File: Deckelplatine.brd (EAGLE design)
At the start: 110 x 75 mm, 61 parts, among them IC1 MAX1487EESA+, IC2 74HCT595D, IC3 74HCT595D, IC4 74HCT595D, IC5 74HCT595D, IC6 74HCT595D, J1 52808-2570, Q1 BC846BSMD, Q2 BC846BSMD, U1 LM2676S, X1 236-404, X2 233-502

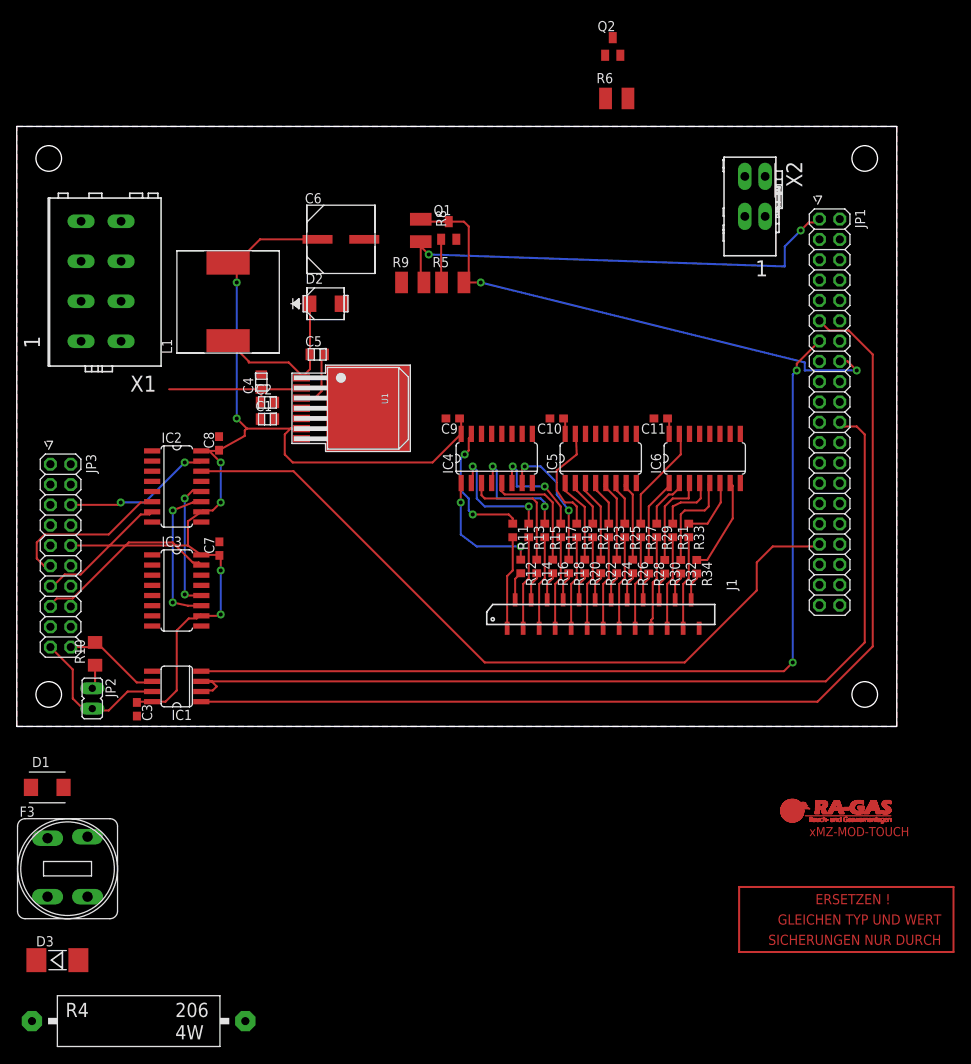
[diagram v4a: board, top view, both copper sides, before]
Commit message: Schema, Board Layout und Routing komplett
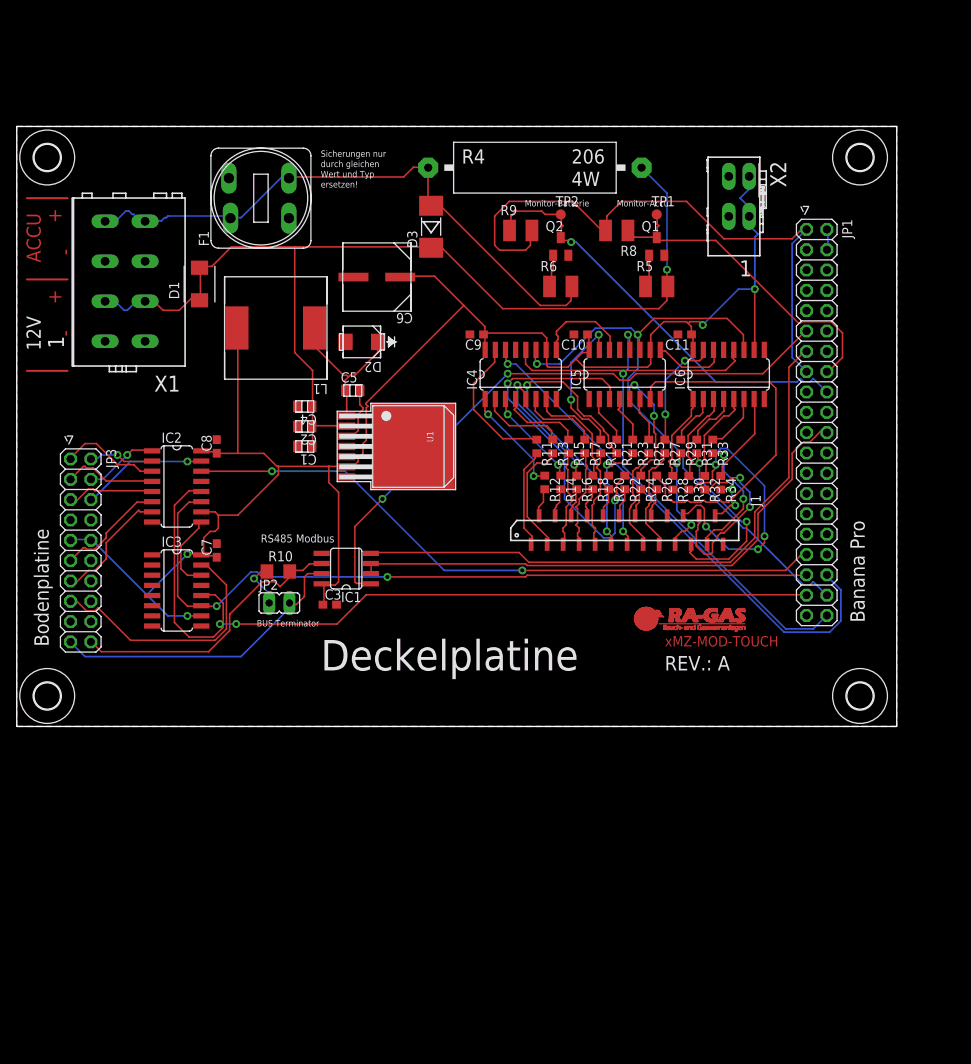
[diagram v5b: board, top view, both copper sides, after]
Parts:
- removed F3: 0.63AT, fuse-schurter:3101.0040
- added F1: FPG4-3101.0040, fuse-schurter:3101.0040
- added H1, H2, H3, H4: MOUNT-HOLE3.3, holes:3,3
- added TP1, TP2: TPSB1,27, testpad:B1,27
- moved R4 117.6 mm to (64.8, 69.8)
- moved D3 102.9 mm to (51.8, 62.5), turned to 90 degrees
- moved D1 65.7 mm to (22.9, 55.3), turned to 90 degrees
- moved C3 27.4 mm to (39.1, 15.2), turned to 0 degrees
- moved JP2 26.3 mm to (32.8, 15.4), turned to 270 degrees
- moved Q1 26.1 mm to (80.0, 60.0)
- moved Q2 25.8 mm to (68.0, 60.0)
- moved IC1 25.8 mm to (41.2, 19.7)
- moved R5 25.5 mm to (80.0, 55.0)
- moved R10 25.1 mm to (32.7, 19.4), turned to 0 degrees
- moved R6 24.5 mm to (68.0, 55.0)
- moved R8 24.5 mm to (75.0, 62.0), turned to 180 degrees
- moved R9 15.0 mm to (63.0, 62.0)
- moved C10 10.9 mm to (70.5, 49.0)
- moved C11 10.9 mm to (83.5, 49.0)
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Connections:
- removed net ACCU-: X1.L4.1, X1.L4.2
- removed net N$38: D3.A, F3.4, R4.1
- removed net N$39: F3.1
- removed net V+: D3.C, R4.2
- net !MON_BAT: now also TP2.TP; no longer R6.2
- net !MON_MAINS: now also TP1.TP; no longer R5.2
- net 12V_VIN: now also D3.C, R4.2, R5.2, X1.L2.1, X1.L2.2; no longer X1.L1.1, X1.L1.2
- net ACCU+: now also D3.A, F1.1, F1.4, R4.1, R6.2, X1.L4.1, X1.L4.2; no longer X1.L3.1, X1.L3.2
- net GND: now also X1.L1.1, X1.L1.2, X1.L3.1, X1.L3.2; no longer X1.L2.1, X1.L2.2
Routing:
- net 12V_VIN: track 18.1 -> 129.6 mm, vias 0 -> 1
- net REL_RCK: track 16.7 -> 107.6 mm
- net LED_RCK: track 0.00 -> 84.1 mm, vias 0 -> 2
- net VCC: track 144.8 -> 226.0 mm, vias 6 -> 4
- net LED_SCK: track 0.00 -> 80.4 mm, vias 0 -> 2
- net REL_SCK: track 18.9 -> 95.2 mm
- net ACCU+: track 0.00 -> 74.3 mm
- net N$1413: track 69.8 -> 0.00 mm
- net LED_SER: track 0.00 -> 64.5 mm, vias 0 -> 1
- net RXD: track 131.7 -> 76.2 mm, vias 0 -> 2
- net !MON_BAT: track 0.00 -> 53.6 mm, vias 0 -> 1
- net RTS: track 118.9 -> 69.1 mm
- net TXD: track 115.9 -> 76.0 mm, vias 2 -> 0
- net N$17: track 10.4 -> 48.8 mm, vias 0 -> 2
- net N$22: track 10.1 -> 46.2 mm
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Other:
- board text added: "+"
- board text added: "-"
- board text added: "12V"
- board text added: "ACCU"
- board text added: "BUS Terminator"
- board text added: "Banana Pro"
- board text added: "Bodenplatine"
- board text added: "Deckelplatine"
- board text added: "Monitor-Accu"
- board text added: "Monitor-Batterie"
- board text added: "REV.: A"
- board text added: "RS485 Modbus"
- board text added: "Sicherungen nur durch gleichen Wert und Typ ersetzen!"
- board text removed: "ERSETZEN !"
- board text removed: "GLEICHEN TYP UND WERT"
- board text removed: "SICHERUNGEN NUR DURCH"

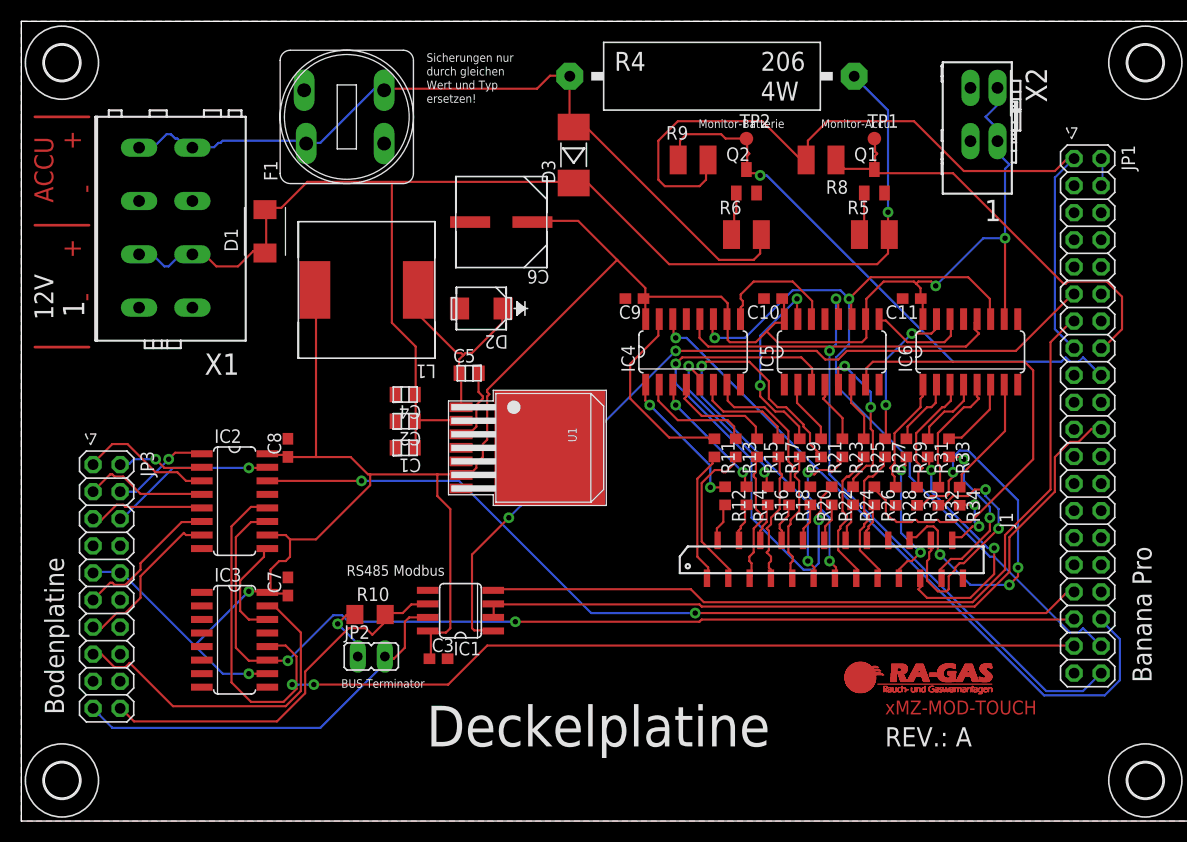
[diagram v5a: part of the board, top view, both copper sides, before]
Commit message: Autorouter mit 7 Airwire left
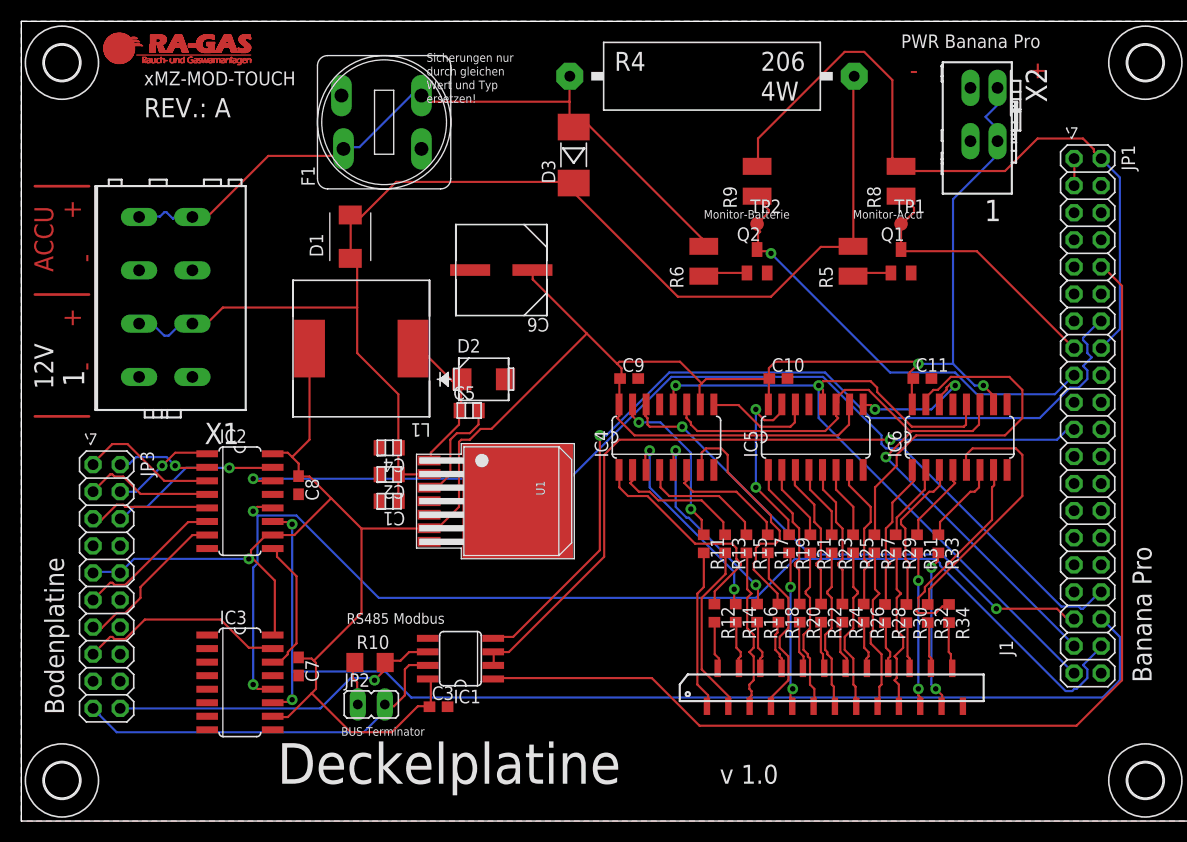
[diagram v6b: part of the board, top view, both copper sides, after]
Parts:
- moved J1 12.0 mm to (76.0, 12.5)
- moved R12 11.0 mm to (65.0, 19.5)
- moved R14 11.0 mm to (67.0, 19.5)
- moved R16 11.0 mm to (69.0, 19.5)
- moved R18 11.0 mm to (71.0, 19.5)
- moved R20 11.0 mm to (73.0, 19.5)
- moved R22 11.0 mm to (75.0, 19.5)
- moved R24 11.0 mm to (77.0, 19.5)
- moved R26 11.0 mm to (79.0, 19.5)
- moved R28 11.0 mm to (81.0, 19.5)
- moved R30 11.0 mm to (83.0, 19.5)
- moved R32 11.0 mm to (85.0, 19.5)
- moved R34 11.0 mm to (87.0, 19.5)
- moved R11 9.06 mm to (64.0, 26.0)
- moved R13 9.06 mm to (66.0, 26.0)
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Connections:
- new net N$1415: JP1.12
- net !MON_BAT: now also JP1.17; no longer JP1.18
- net !MON_MAINS: now also JP1.15; no longer JP1.16
- net GND: now also JP1.13, JP1.26, JP1.33, JP1.40, JP1.5; no longer JP1.14, JP1.25, JP1.34, JP1.39, JP1.6, JP1.9
- net LED_RCK: now also JP1.39; no longer JP1.40
- net LED_SCK: now also JP1.37; no longer JP1.38
- net LED_SER: now also JP1.35; no longer JP1.36
- net REL_RCK: now also JP1.38; no longer JP1.37
- net REL_SCK: now also JP1.36; no longer JP1.35
- net REL_SER: now also JP1.34; no longer JP1.33
- net RTS: now also JP1.21; no longer JP1.22
- net RXD: now also JP1.10; no longer JP1.11
- net TXD: now also JP1.14; no longer JP1.13
- net VCC3.3V: now also JP1.16, JP1.2; no longer JP1.1, JP1.15
- net VCC5V: now also JP1.1, JP1.3; no longer JP1.2, JP1.4
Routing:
- net N$17: track 48.8 -> 14.0 mm, vias 2 -> 0
- net D20: track 37.3 -> 4.41 mm, vias 4 -> 0
- net N$22: track 46.2 -> 14.1 mm
- net RXD: track 76.2 -> 102.3 mm, vias 2 -> 0
- net D11: track 41.1 -> 15.4 mm, vias 2 -> 0
- net VCC: track 226.0 -> 249.1 mm, vias 4 -> 3
- net N$23: track 14.3 -> 35.2 mm, vias 2 -> 0
- net D22: track 23.5 -> 4.44 mm, vias 2 -> 0
- net LED_SCK: track 80.4 -> 64.7 mm, vias 2 -> 1
- net !MON_MAINS: track 41.2 -> 26.2 mm
- net LED_SER: track 64.5 -> 49.6 mm, vias 1 -> 2
- net N$15: track 0.00 -> 14.1 mm
- net REL_SER: track 81.6 -> 95.6 mm, vias 2 -> 1
- net N$28: track 11.8 -> 25.0 mm
- net P9: track 32.1 -> 19.5 mm
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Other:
- board text added: ">VERSION"
- board text added: "PWR Banana Pro"
- board text added: "v"

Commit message: Routing fertig, keine Airwires übrig
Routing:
- net VCC: track 249.1 -> 257.3 mm
- net LED_RCK: track 72.1 -> 76.2 mm
- net N$28: track 25.0 -> 28.6 mm
- net LED_SCK: track 64.7 -> 66.5 mm
- net N$13: track 23.3 -> 25.1 mm
- net N$23: track 35.2 -> 34.6 mm

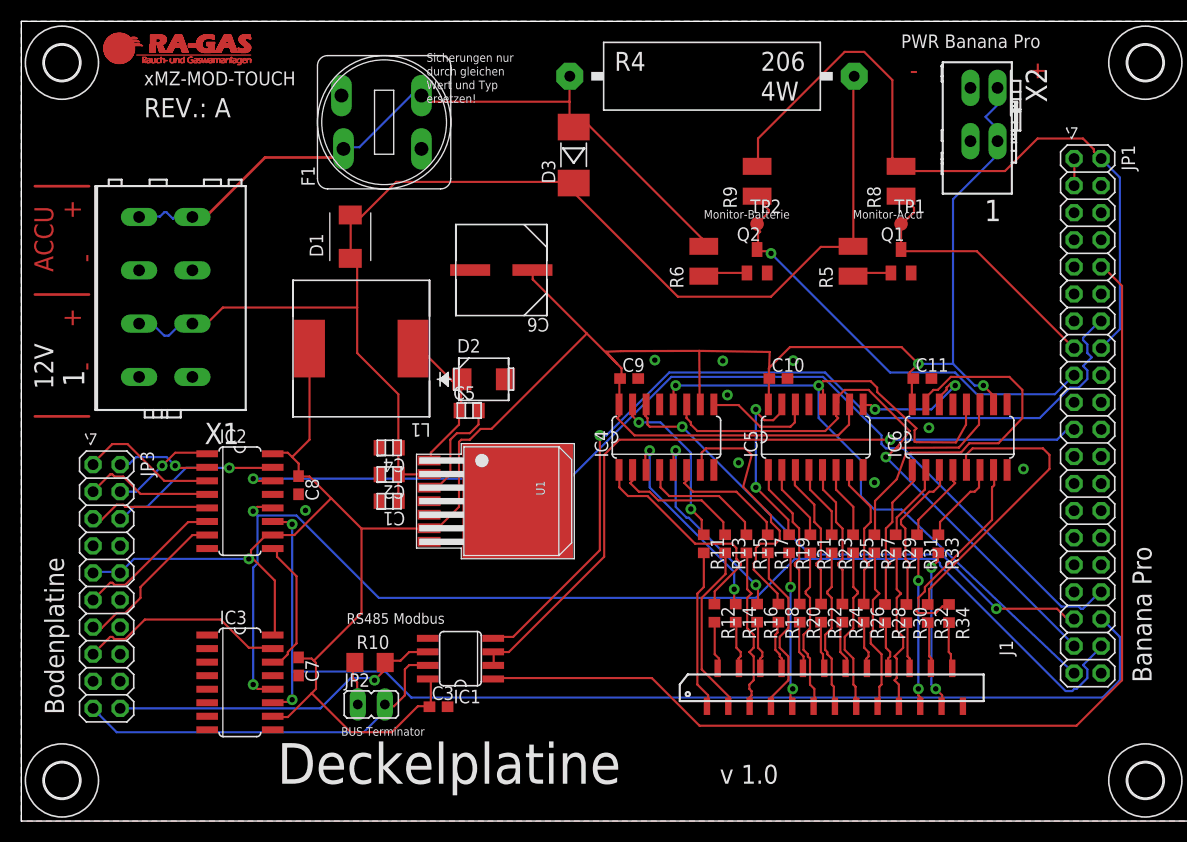
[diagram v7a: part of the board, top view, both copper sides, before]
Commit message: Erste ferige Version nach Tausch der Sicherung
Board Layout, Schema, dicke Power Lines, neue Sicherung
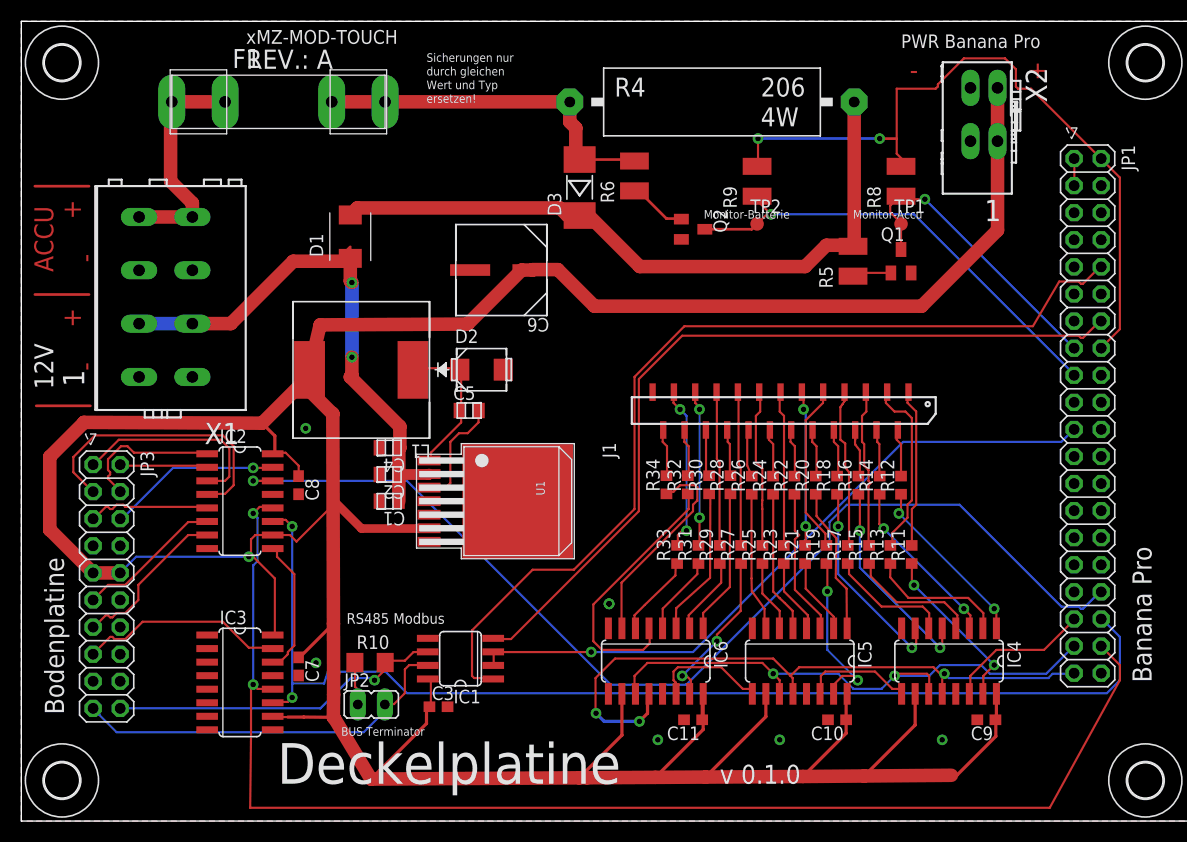
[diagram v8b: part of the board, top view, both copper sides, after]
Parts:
- F1: value FPG4-3101.0040 -> 01110005MR; device fuse-schurter:3101.0040 -> fuse-littlefuse:01110005MR
- moved C9 46.3 mm to (90.5, 9.50), turned to 180 degrees
- moved C11 38.6 mm to (63.0, 9.50), turned to 180 degrees
- moved IC6 35.4 mm to (59.5, 15.0), turned to 180 degrees
- moved IC4 33.8 mm to (87.0, 15.0), turned to 180 degrees
- moved C10 32.5 mm to (76.5, 9.50), turned to 180 degrees
- moved R34 29.1 mm to (60.5, 31.5), turned to 90 degrees
- moved J1 26.4 mm to (71.5, 38.5), turned to 270 degrees
- moved R32 25.5 mm to (62.5, 31.5), turned to 90 degrees
- moved R33 24.5 mm to (61.5, 25.0), turned to 90 degrees
- moved R30 22.1 mm to (64.5, 31.5), turned to 90 degrees
- moved R12 21.2 mm to (82.5, 31.5), turned to 90 degrees
- moved IC5 21.1 mm to (73.0, 15.0), turned to 180 degrees
- moved R31 20.5 mm to (63.5, 25.0), turned to 90 degrees
- moved R11 19.5 mm to (83.5, 25.0), turned to 90 degrees
- moved R28 18.9 mm to (66.5, 31.5), turned to 90 degrees
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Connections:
- net ACCU+: now also F1.1A, F1.1B, F1.2A, F1.2B; no longer F1.1, F1.4
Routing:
- net VCC: track 257.3 -> 358.9 mm, vias 3 -> 1
- net LED_SER: track 49.6 -> 13.7 mm, vias 2 -> 0
- net N$23: track 34.6 -> 15.3 mm, vias 0 -> 2
- net RXD: track 102.3 -> 87.6 mm
- net LED_RCK: track 76.2 -> 61.5 mm, vias 2 -> 3
- net P5: track 12.1 -> 26.8 mm
- net ACCU+: track 68.3 -> 55.1 mm
- net LED_SCK: track 66.5 -> 54.1 mm, vias 1 -> 2
- net REL_RCK: track 112.9 -> 124.8 mm
- net N$778: track 10.7 -> 0.00 mm
- net 12V_VIN: track 125.0 -> 116.6 mm, vias 0 -> 2
- net REL_SER: track 95.6 -> 102.1 mm
- net P4: track 13.0 -> 19.0 mm
- net TXD: track 82.8 -> 76.9 mm, vias 1 -> 0
- net N$13: track 25.1 -> 19.3 mm, vias 0 -> 2
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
